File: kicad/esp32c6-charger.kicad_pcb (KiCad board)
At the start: 2 copper layers, 160 x 50 mm, 17 parts, among them J1 Conn_01x06_Socket, J2 Conn_01x03_Socket, K1 G2RL-1, Q1 BC817, Q2 BC817, U1 XIAO-ESP32-C6

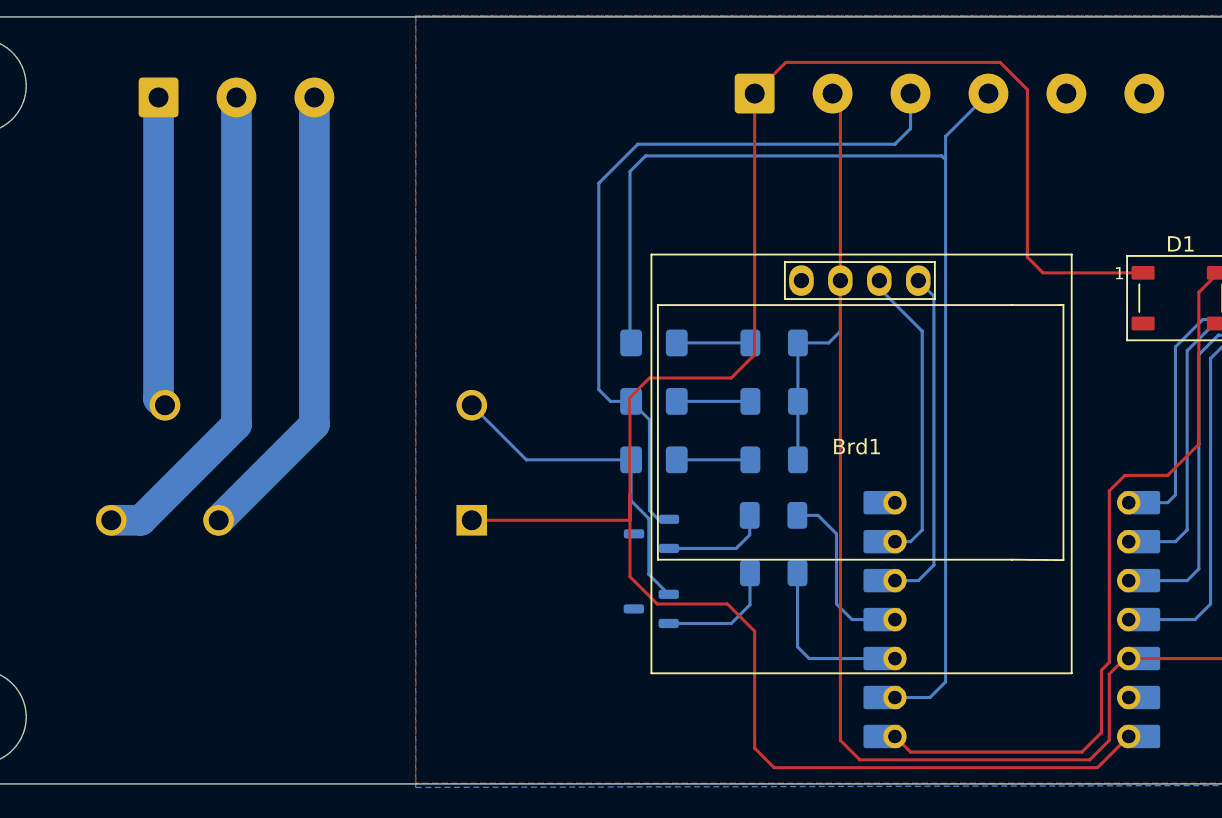
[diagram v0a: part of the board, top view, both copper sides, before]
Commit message: added external power possibility
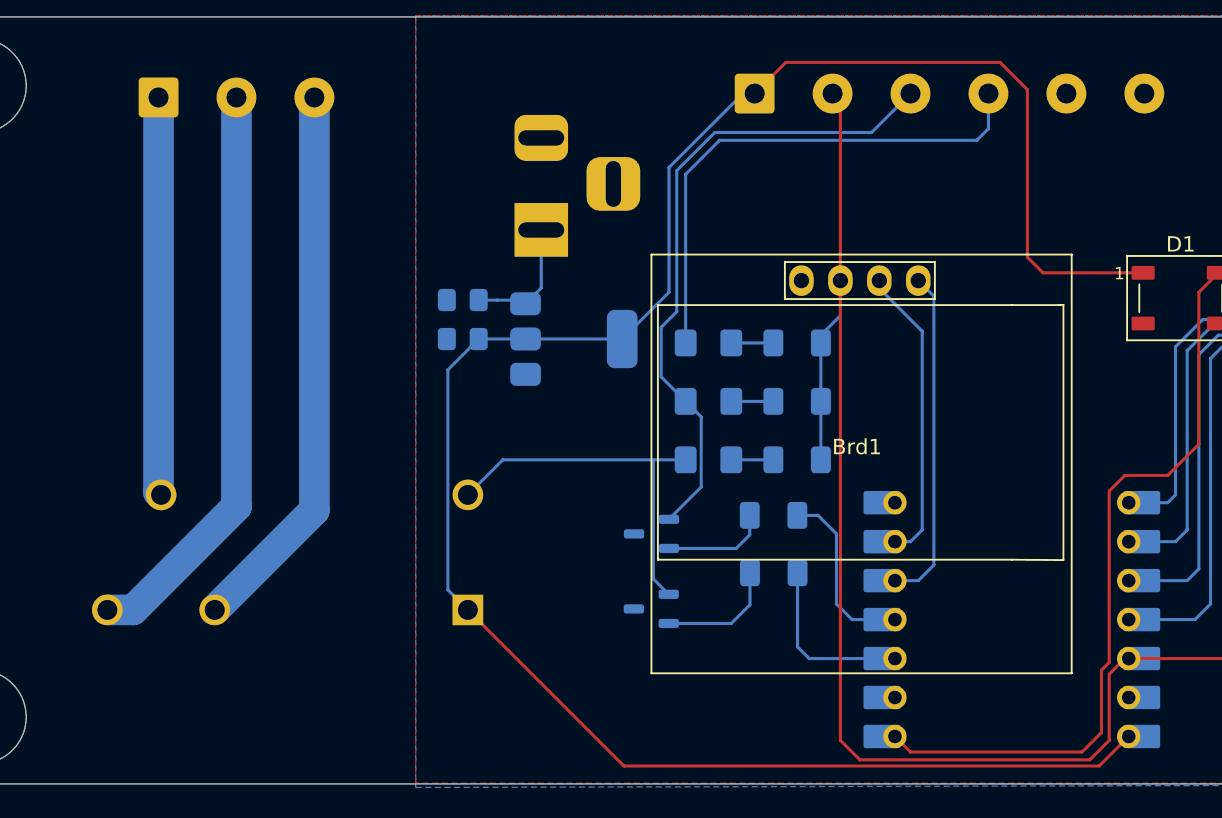
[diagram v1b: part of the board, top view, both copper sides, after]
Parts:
- added C1: 10uF, Capacitor_SMD:C_0805_2012Metric_Pad1.18x1.45mm_HandSolder, B.Cu at (105.7, 108.5)
- added C2: 22uF, Capacitor_SMD:C_0805_2012Metric_Pad1.18x1.45mm_HandSolder, B.Cu at (105.7, 111.0)
- added J3: Conn_Coaxial_Power, Connector_BarrelJack:BarrelJack_Horizontal, B.Cu at (110.8, 103.9)
- added U2: AMS1117-5.0, Package_TO_SOT_SMD:SOT-223-3_TabPin2, B.Cu at (112.9, 111.0)
- moved K1 5.85 mm to (106.0, 128.7)
- moved D2 3.56 mm to (121.7, 115.1)
- moved D3 3.56 mm to (121.7, 118.9)
- moved D4 3.56 mm to (121.7, 111.3)
- moved R3 1.50 mm to (127.5, 118.9)
- moved R4 1.50 mm to (127.5, 115.1)
- moved R5 1.50 mm to (127.5, 111.3)
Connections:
- net +5V renamed VDD
- net Net-(D1-DIN) renamed /LED
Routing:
- net Net-(D4-K): track 76.4 -> 35.1 mm
- net +12V: track 0.00 -> 8.39 mm
- net Net-(D2-K): track 49.1 -> 42.4 mm
- net Net-(J2-Pin_3): track 29.4 -> 35.3 mm
- net Net-(J2-Pin_2): track 31.7 -> 37.1 mm
- net Net-(J2-Pin_1): track 20.1 -> 25.2 mm
- net VDD: track 131.2 -> 134.7 mm
- net Net-(D3-K): track 21.7 -> 24.3 mm
- net Net-(D4-A): track 4.80 -> 2.74 mm
- net Net-(D3-A): track 4.80 -> 2.74 mm
- net Net-(D2-A): track 4.80 -> 2.74 mm
- net VCC: track 103.0 -> 101.2 mm

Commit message: updated changes to schematic and pcb
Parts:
- C1, C2: footprint Capacitor_SMD:C_0805_2012Metric_Pad1.18x1.45mm_HandSolder -> Capacitor_Tantalum_SMD:CP_EIA-6032-28_Kemet-C
- J1: value Conn_01x06_Socket -> Power/Lock/Detect
- J2: value Conn_01x03_Socket -> Relay
- R3, R4, R5: value 68 -> 68Ω
- moved R2 2.65 mm to (125.2, 128.8)
- moved C2 2.30 mm to (105.9, 113.3)
- moved U2 1.85 mm to (114.7, 111.5)
- moved R1 1.63 mm to (125.2, 124.0)
- moved R3 1.57 mm to (129.0, 118.6)
- moved R4 1.57 mm to (129.0, 114.8)
- moved R5 1.57 mm to (129.0, 111.0)
- moved D3 1.57 mm to (123.3, 118.6)
- moved D2 1.57 mm to (123.3, 114.8)
- moved D4 1.57 mm to (123.3, 111.0)
- moved C1 0.80 mm to (105.9, 109.2)
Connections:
- net Net-(D2-K) renamed /Lock
- net Net-(D4-K) renamed /Detect
- J3 pad 3: GND -> (no net)
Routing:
- net Net-(D3-K): track 24.3 -> 28.8 mm
- net Net-(Q2-B): track 7.88 -> 4.85 mm
- net Net-(Q1-B): track 7.53 -> 4.58 mm
- net Net-(U1-GPIO2/A2/D2): track 10.9 -> 8.86 mm
- net +12V: track 8.39 -> 10.1 mm
- net VDD: track 134.7 -> 133.8 mm
- net /Detect: track 35.1 -> 36.0 mm
- net /Lock: track 42.4 -> 43.2 mm
- net VCC: track 101.2 -> 100.6 mm

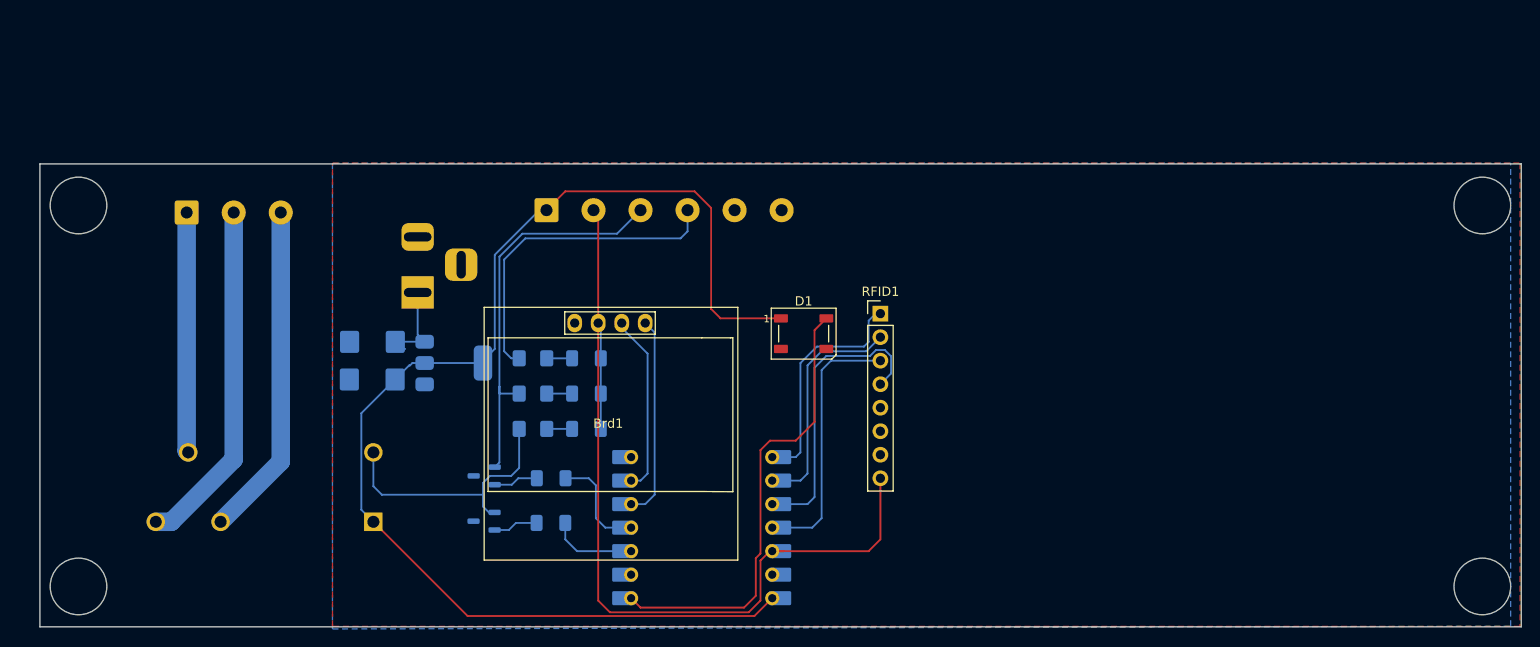
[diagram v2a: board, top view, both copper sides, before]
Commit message: small changes and a pdf of the schematic in the export jobset
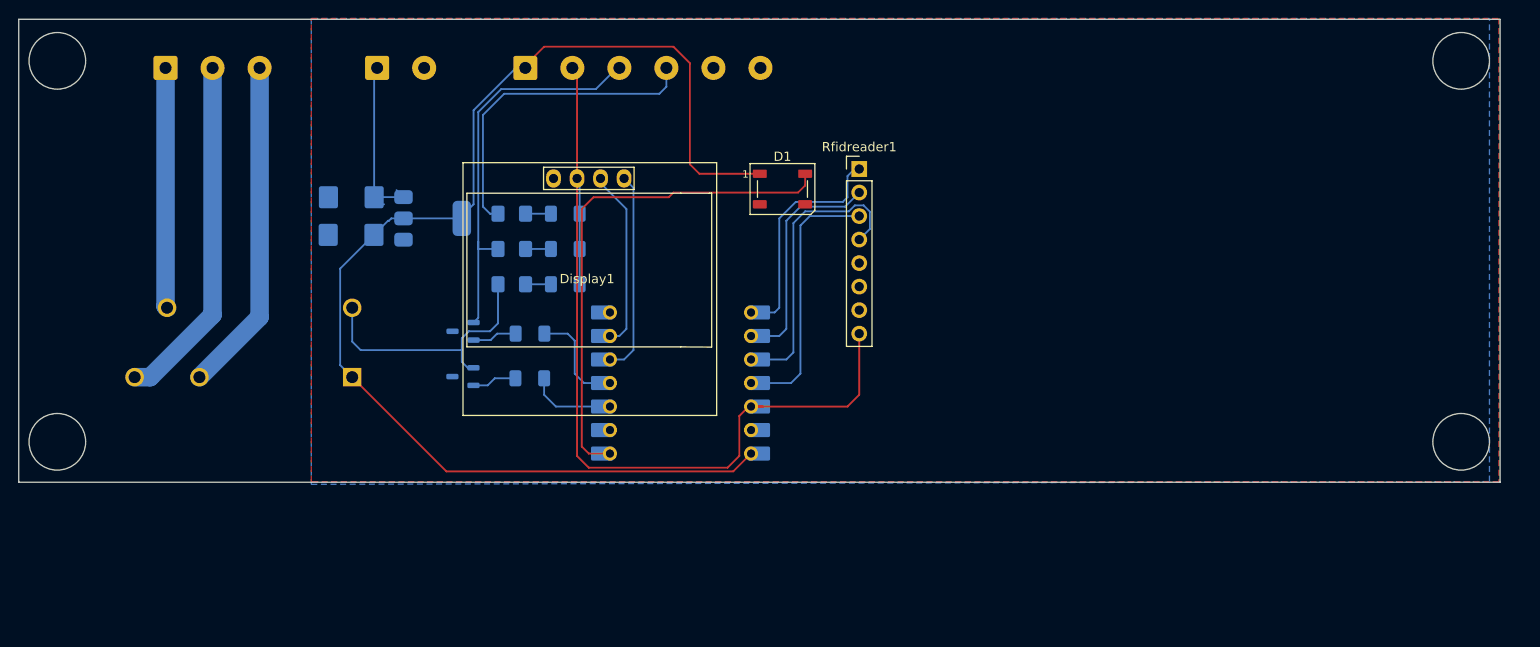
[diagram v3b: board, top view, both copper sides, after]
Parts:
- removed the J3 at (110.8, 103.9)
- added J1: Conn_01x02_Socket, TerminalBlock_Phoenix:TerminalBlock_Phoenix_MKDS-1,5-2-5.08_1x02_P5.08mm_Horizontal, B.Cu at (106.4, 79.6)
- moved R4 15.8 mm to (126.7, 99.2)
- moved R5 15.8 mm to (126.7, 95.4)
- moved C2 15.8 mm to (103.6, 97.7)
- moved D3 15.8 mm to (121.0, 99.2)
- moved D4 15.8 mm to (121.0, 95.4)
- moved Q1 15.8 mm to (115.7, 113.0)
- moved R3 15.8 mm to (126.7, 103.0)
- moved C1 15.8 mm to (103.6, 93.6)
- moved D1 15.8 mm to (150.2, 92.7)
- moved D2 15.8 mm to (121.0, 103.0)
- moved Display1 15.8 mm to (129.1, 102.2)
- moved J3 15.8 mm to (83.6, 79.6)
- moved K1 15.8 mm to (103.7, 113.0)
- moved Q2 15.8 mm to (115.7, 108.1)
- moved R1 15.8 mm to (122.9, 113.2)
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- renumbered D3 to D2, D2 to D3, Brd1 to Display1, J1 to J2, J2 to J3, Q2 to Q1, Q1 to Q2, R2 to R1, R1 to R2, RFID1 to Rfidreader1, U2 to U1, U1 to U2
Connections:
- net Net-(D3-K) renamed /Relay
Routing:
- net +12V: track 10.1 -> 19.9 mm
- net /LED: track 49.2 -> 55.5 mm
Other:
- board text added: "~12V"

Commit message: updated 3d model for relay
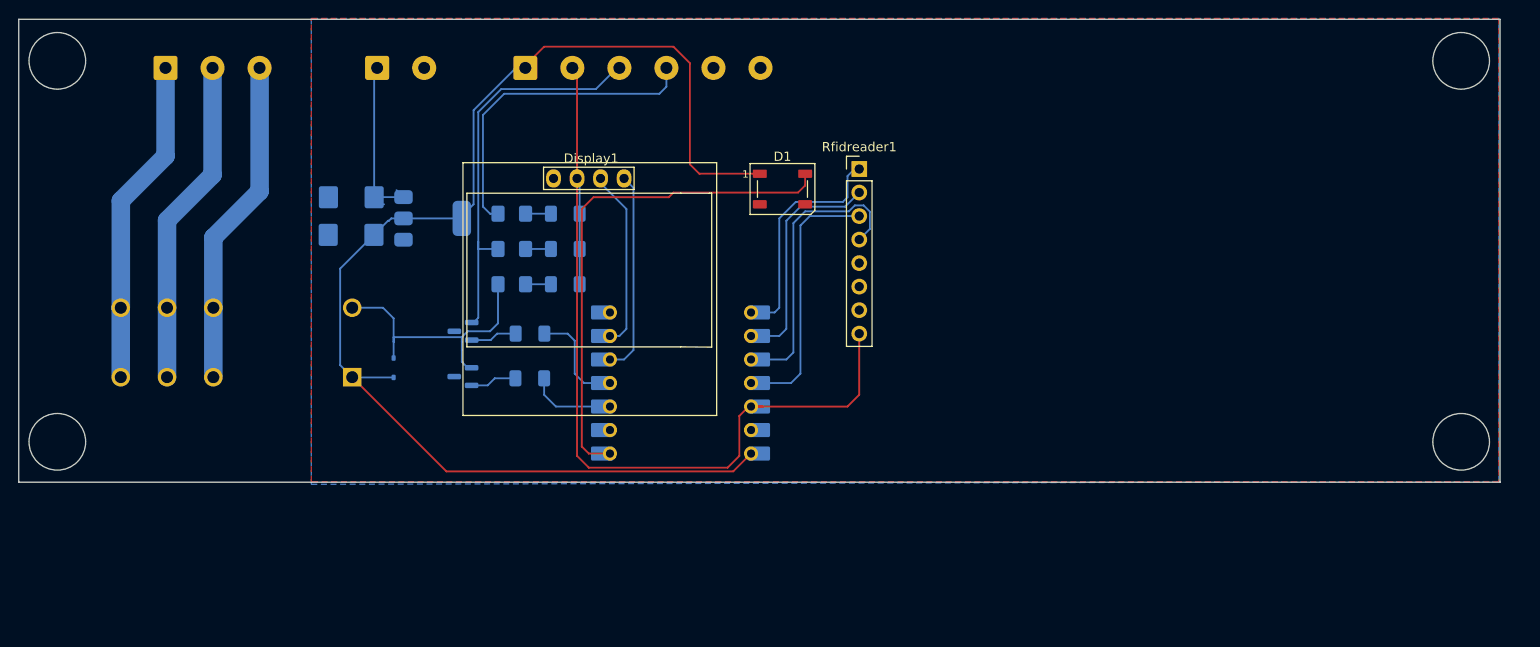
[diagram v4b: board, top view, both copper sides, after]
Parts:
- added D5: 1N4148WS, Diode_SMD:D_SOD-323, B.Cu at (108.2, 112.0)
- K1: footprint Relay_THT:Relay_SPDT_Omron_G2RL-1 -> Relay_THT:Relay_SPDT_Omron_G2RL-1-E
- Q1, Q2: footprint Package_TO_SOT_SMD:SOT-23-3 -> Package_TO_SOT_SMD:SOT-23
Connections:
- K1 pad 11: Net-(J3-Pin_1) -> Net-(J3-Pin_2)
- K1 pad 14: Net-(J3-Pin_2) -> Net-(J3-Pin_1)
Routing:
- net Net-(J3-Pin_1): track 25.2 -> 35.4 mm
- net VDD: track 133.8 -> 138.3 mm
- net Net-(J3-Pin_2): track 37.1 -> 35.4 mm
- net /Relay: track 28.8 -> 30.1 mm

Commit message: small changes to copper
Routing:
- net /Detect: track 36.0 -> 70.5 mm
- net /Relay: track 30.1 -> 35.8 mm
- net Net-(U2-GPIO2/A2/D2): track 8.86 -> 6.37 mm
- net +12V: track 19.9 -> 17.5 mm
- net /Lock: track 43.2 -> 42.1 mm

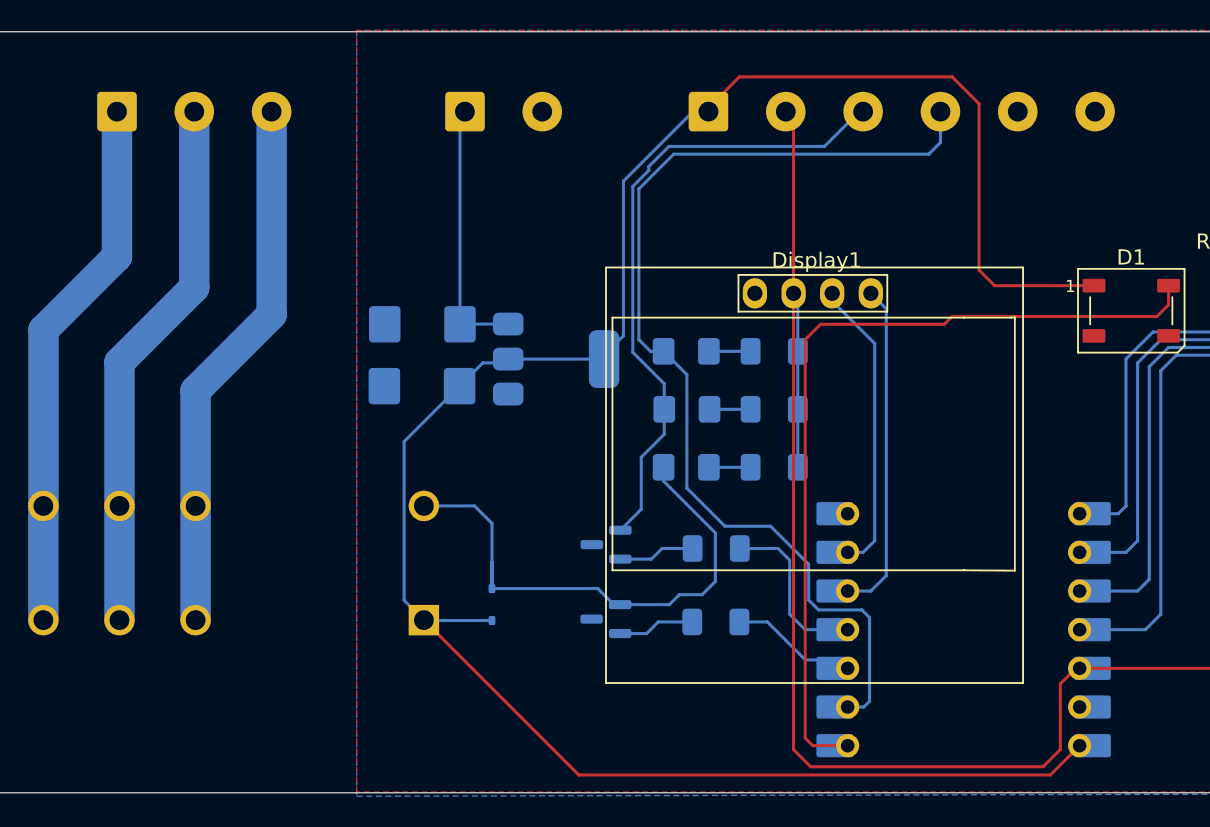
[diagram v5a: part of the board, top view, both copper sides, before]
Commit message: used normal transistors and diodes instead of SMD ones, we have the space, why make soldering life more difficult
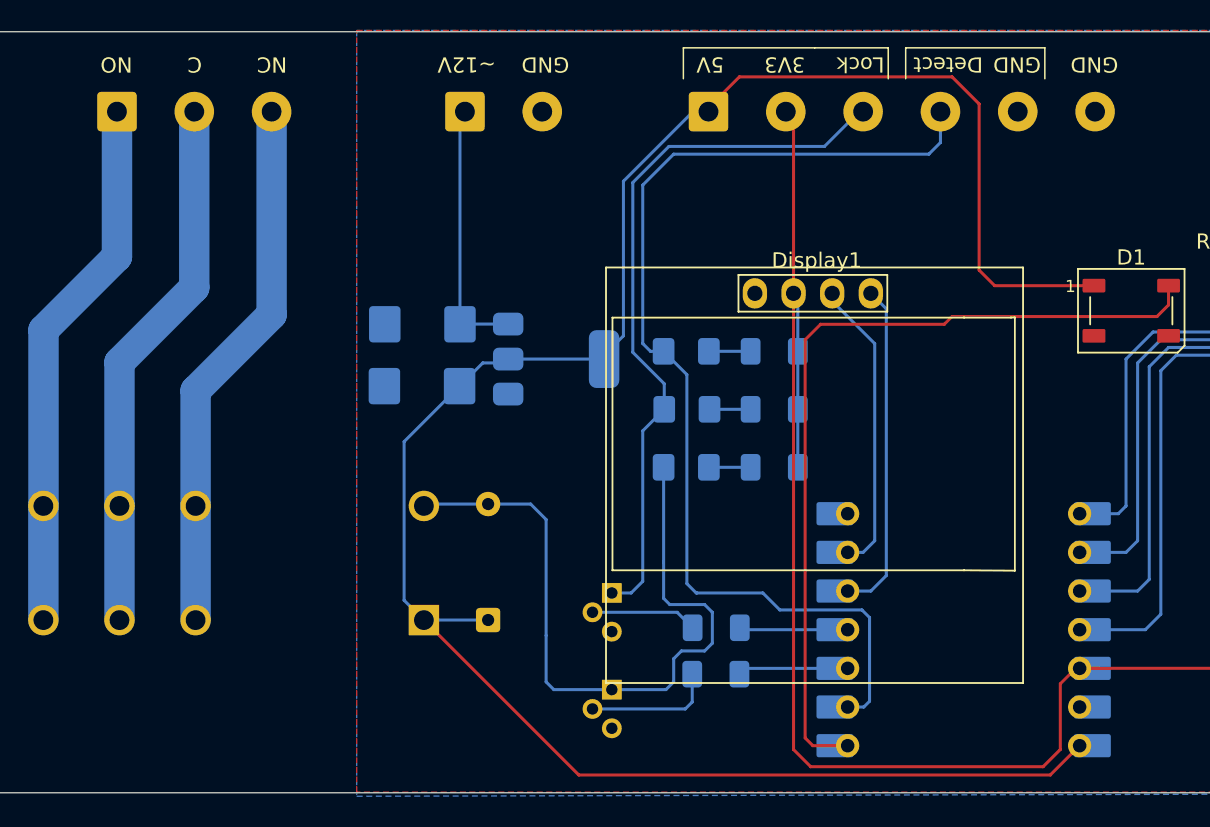
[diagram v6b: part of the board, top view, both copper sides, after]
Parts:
- D5: footprint Diode_SMD:D_SOD-323 -> Diode_THT:D_DO-35_SOD27_P7.62mm_Horizontal
- Q1, Q2: value BC817 -> BC337; footprint Package_TO_SOT_SMD:SOT-23 -> Package_TO_SOT_THT:TO-92
- moved R2 5.21 mm to (122.9, 113.5)
- moved Q1 4.65 mm to (116.1, 117.6), turned to -90 degrees
- moved R1 3.43 mm to (122.9, 116.6)
- moved Q2 3.20 mm to (116.1, 111.3), turned to -90 degrees
- moved D5 1.05 mm to (108.0, 113.0)
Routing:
- net /Relay: track 35.8 -> 46.7 mm
- net /Lock: track 42.1 -> 47.2 mm
- net Net-(U2-GPIO21/D3): track 10.8 -> 6.30 mm
- net Net-(Q1-B): track 4.85 -> 8.98 mm
- net Net-(Q2-B): track 4.58 -> 7.36 mm
- net /Detect: track 70.5 -> 72.6 mm
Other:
- board text added: "C"
- board text added: "NC"
- board text added: "NO"
